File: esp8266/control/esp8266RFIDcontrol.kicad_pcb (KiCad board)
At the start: 2 copper layers, 33.5 x 68.6 mm, 21 parts, among them J1 C_DOOR, J2 C_STRIKE, J3 Conn_01x05, J4 C_PWR, J5 Barrel_Jack, K1 RTE24005F, Q1 Q_PNP, SW1 SW_RESET, U1 TPS561208, U2 LoLinESP8266

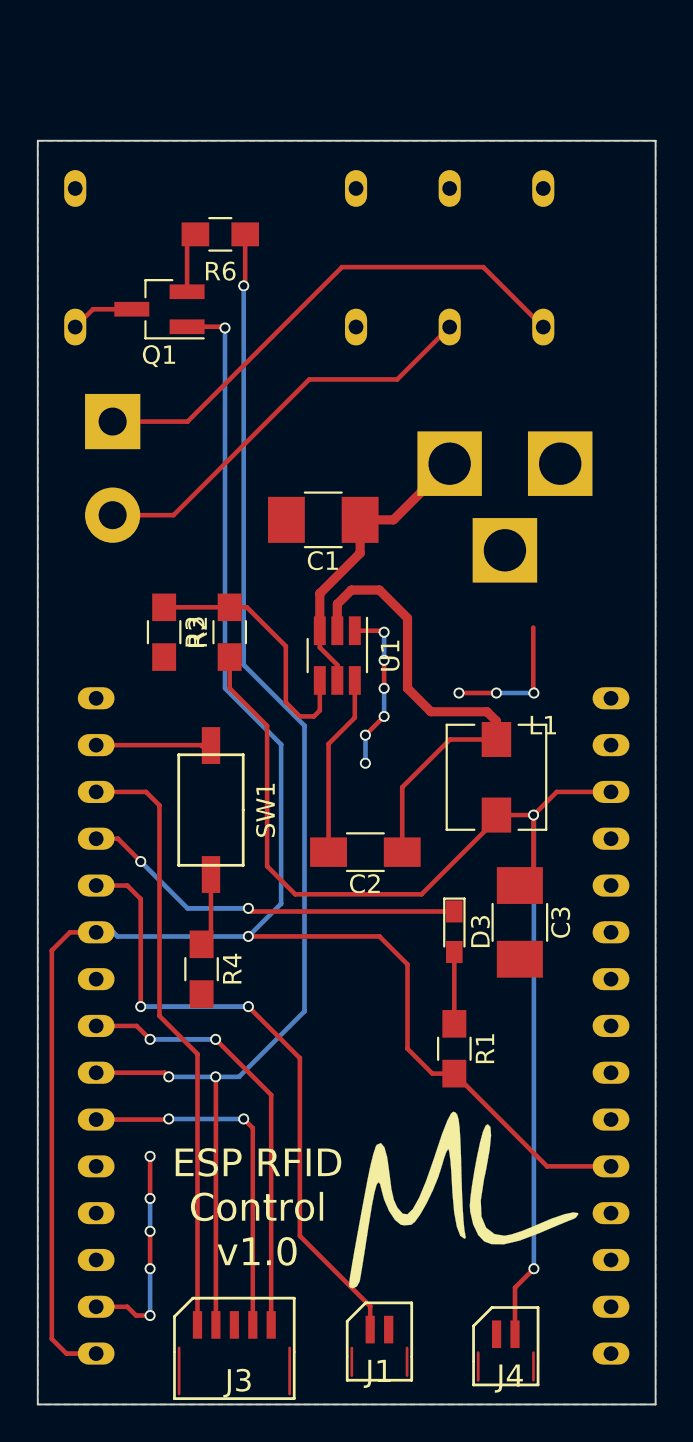
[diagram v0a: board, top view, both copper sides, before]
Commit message: ESP8266 RFID reader board
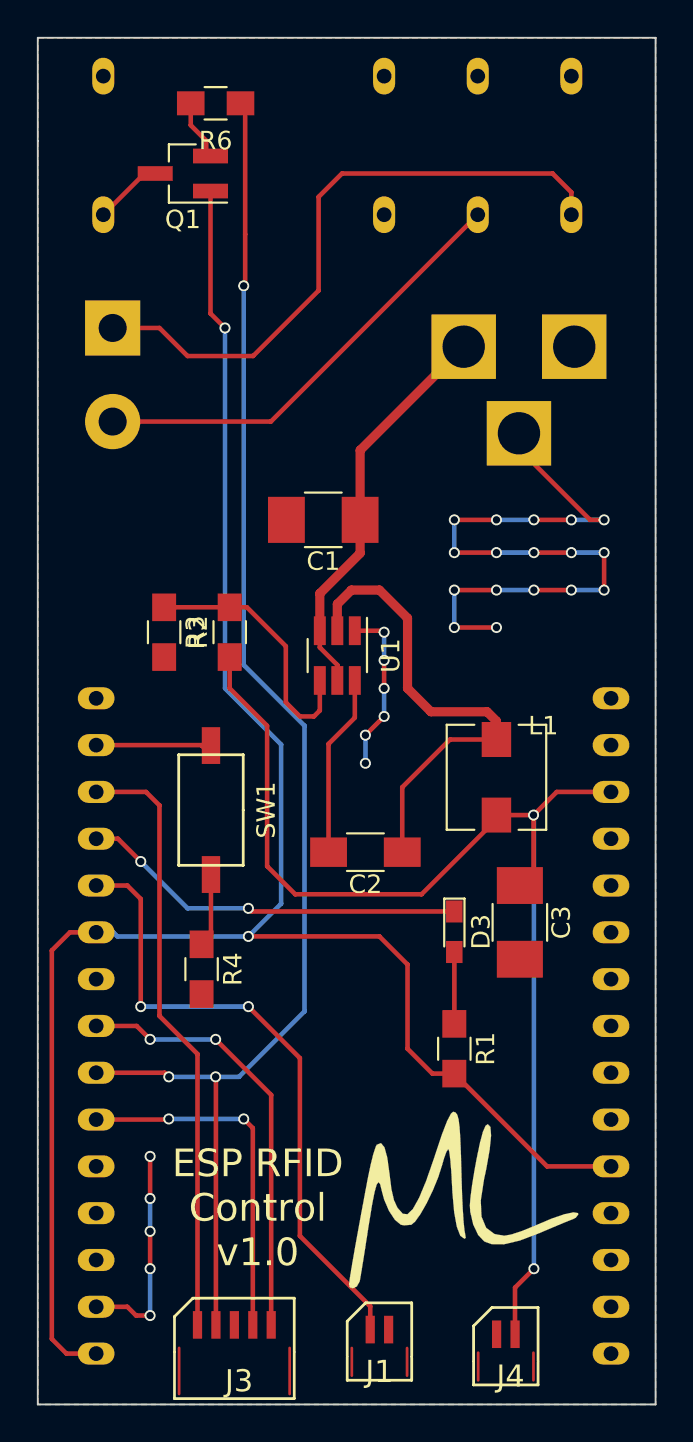
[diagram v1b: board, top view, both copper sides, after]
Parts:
- moved Q1 7.47 mm to (105.7, 65.8)
- moved R6 7.12 mm to (107.4, 62.0)
- moved J5 6.40 mm to (120.9, 75.2)
- moved K1 6.28 mm to (114.0, 64.3)
- moved J2 5.08 mm to (101.9, 74.2)
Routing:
- net GND: track 20.9 -> 60.5 mm, vias 11 -> 28
- net Net-(J2-Pad1): track 28.4 -> 36.3 mm
- net (no net): track 7.63 -> 0.00 mm, vias 3 -> 0
- net D6: track 69.9 -> 77.1 mm
- net +3V3: track 99.6 -> 105.3 mm
- net +12V: track 16.2 -> 21.8 mm
- net Net-(J2-Pad2): track 22.5 -> 24.7 mm
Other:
- board size 33.5 x 68.6 mm -> 33.5 x 74.2 mm
